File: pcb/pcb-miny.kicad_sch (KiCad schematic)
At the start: 109 parts, among them SW1 Switch, SW10 Switch, SW11 Switch, SW12 Switch, SW13 Switch, SW14 Switch, SW15 Switch, SW16 Switch, SW17 Switch, SW18 Switch, SW19 Switch, SW2 Switch, SW20 Switch, SW21 Switch, SW22 Switch, SW23 Switch, SW24 Switch, SW25 Switch, SW26 Switch, SW27 Switch, SW28 Switch, SW29 Switch, SW3 Switch, SW30 Switch, SW31 Switch, SW32 Switch, SW33 Switch, SW34 Switch, SW4 Switch, SW5 Switch, SW6 Switch, SW7 Switch, SW8 Switch, SW9 Switch

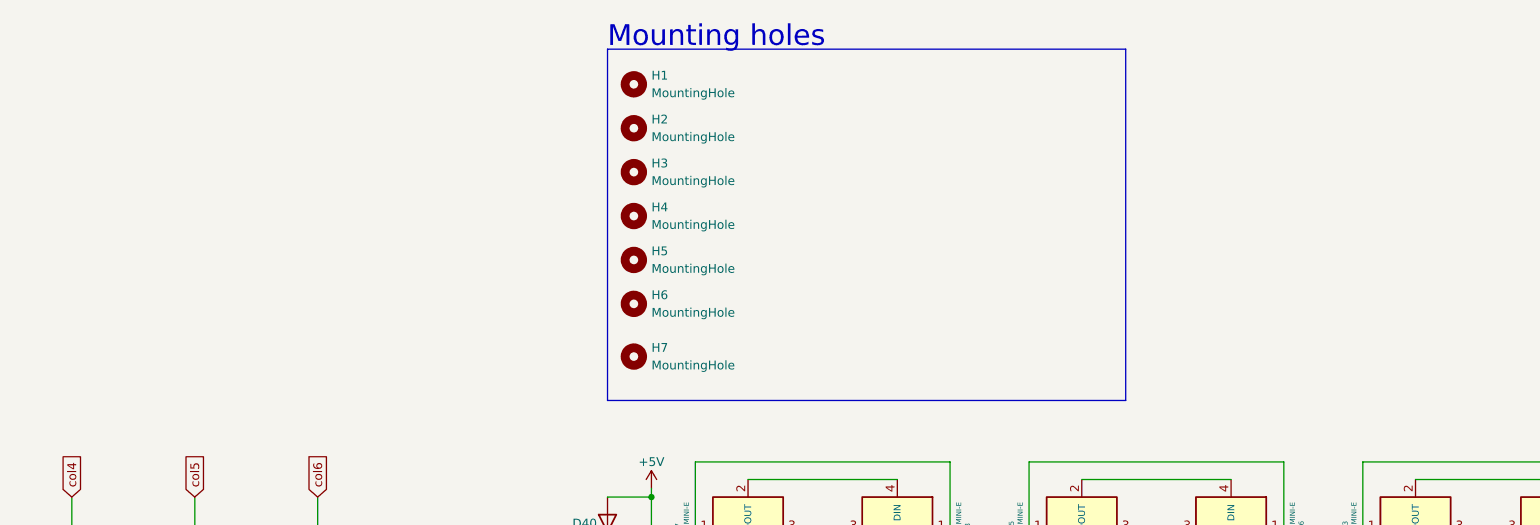
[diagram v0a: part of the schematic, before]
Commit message: add decoupling capacitors
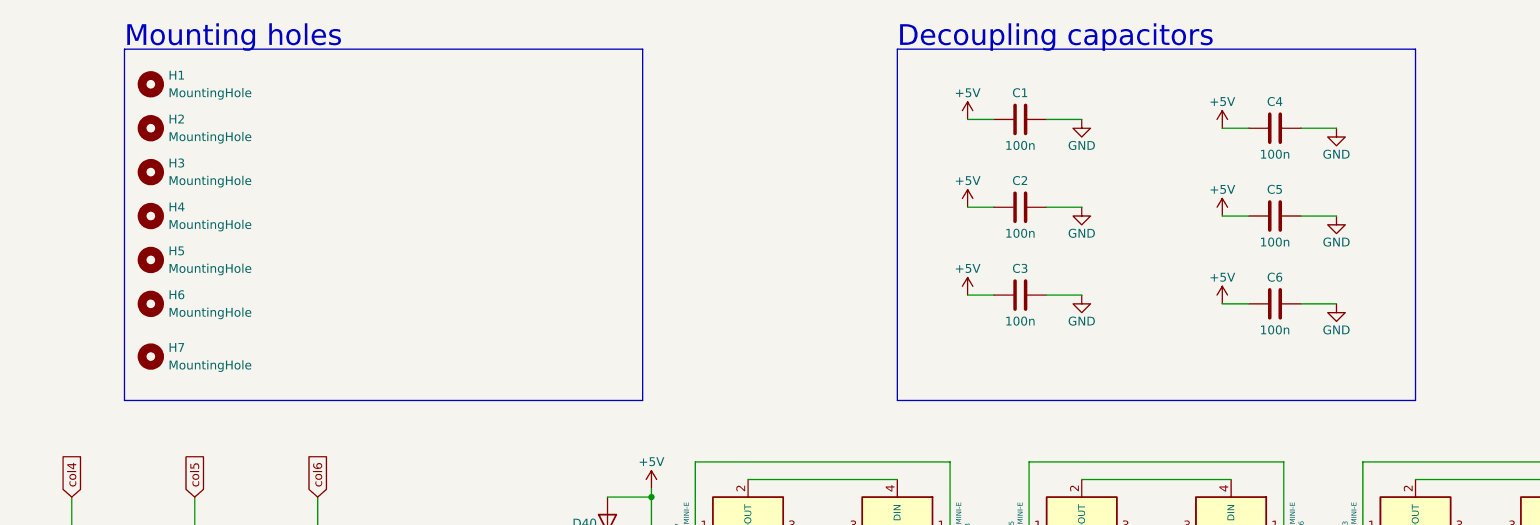
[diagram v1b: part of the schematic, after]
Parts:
- added C1, C2, C3, C4, C5, C6: 100n, Capacitor_SMD:C_1206_3216Metric_Pad1.33x1.80mm_HandSolder, symbol Device:C
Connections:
- net +5V: now also C1.1, C2.1, C3.1, C4.1, C5.1, C6.1
- net GND: now also C1.2, C2.2, C3.2, C4.2, C5.2, C6.2
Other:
- note added: "Decoupling capacitors"
- moved on the sheet: H1, H2, H3, H4, H5, H6, H7
